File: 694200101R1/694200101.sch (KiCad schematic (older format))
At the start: 262 parts, among them J1 USB4085-GF-A, J2 Conn_01x05_Male, J3 Conn_01x02_Male, SW1 MX_SW, SW10 MX_SW, SW100 MX_SW, SW101 MX_SW, SW102 MX_SW, SW103 MX_SW, SW104 MX_SW, SW105 MX_SW, SW106 MX_SW, SW107 MX_SW, SW11 MX_SW, SW12 MX_SW, SW13 MX_SW, SW14 MX_SW, SW15 MX_SW, SW16 MX_SW, SW17 MX_SW, SW18 MX_SW, SW19 MX_SW, SW2 MX_SW, SW20 MX_SW, SW21 MX_SW, SW22 MX_SW, SW23 MX_SW, SW24 MX_SW, SW25 MX_SW, SW26 MX_SW, SW27 MX_SW, SW28 MX_SW, SW29 MX_SW, SW3 MX_SW, SW30 MX_SW, SW31 MX_SW, SW32 MX_SW, SW33 MX_SW, SW34 MX_SW, SW35 MX_SW, SW36 MX_SW, SW37 MX_SW, SW38 MX_SW, SW39 MX_SW, SW4 MX_SW, SW40 MX_SW, SW41 MX_SW, SW42 MX_SW, SW43 MX_SW, SW44 MX_SW, SW45 MX_SW, SW46 MX_SW, SW47 MX_SW, SW48 MX_SW, SW49 MX_SW, SW5 MX_SW, SW50 MX_SW, SW51 MX_SW, SW52 MX_SW, SW53 MX_SW, SW54 MX_SW, SW55 MX_SW, SW56 MX_SW, SW57 MX_SW, SW58 MX_SW, SW59 MX_SW, SW6 MX_SW, SW60 MX_SW, SW61 MX_SW, SW62 MX_SW, SW63 MX_SW, SW64 MX_SW, SW65 MX_SW, SW66 MX_SW, SW67 MX_SW, SW68 MX_SW, SW69 MX_SW, SW7 MX_SW, SW70 MX_SW, SW71 MX_SW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

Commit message: fucking ship it
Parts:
- gave numbers to parts that had none: 1
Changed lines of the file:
@@
 RST
 $Comp
-L capacitor-lib:CL21A475KAQNNNE C?
+L capacitor-lib:CL21A475KAQNNNE C25
 U 1 1 609A6D18
 P 2850 9500
-F 0 "C?" H 2978 9446 50  0000 L CNN
+F 0 "C25" H 2978 9446 50  0000 L CNN
 F 1 "CL21A475KAQNNNE" H 2850 9700 50  0001 L CNN
 F 2 "Capacitor_SMD:C_0805_2012Metric" H 2850 9800 50  0001 L CNN

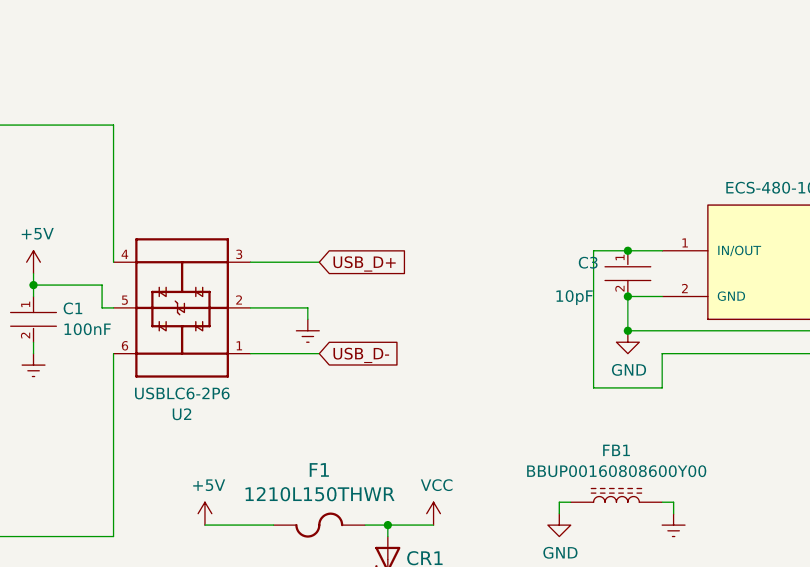
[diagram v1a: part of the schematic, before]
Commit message: Added 0 Ohm resistors for USB Data lines
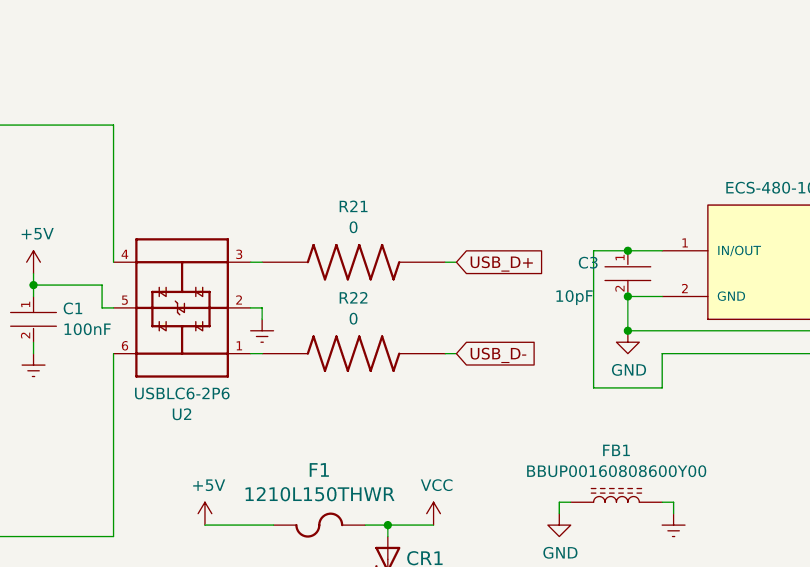
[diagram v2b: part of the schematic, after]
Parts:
- added R21, R22: MCT06030Z0000ZP500, Resistor-Libs:RESC1508X55N, symbol Resistor-Lib:MCT06030Z0000ZP500
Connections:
- net USB_D+: now also R21.2; no longer U2.3
- net USB_D-: now also R22.2; no longer U2.1
- new net: R22.1, U2.1
- new net: R21.1, U2.3
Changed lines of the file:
@@
 Wire Wire Line
 	2400 7950 2400 8950
-Text GLabel 4250 7350 2    50   Input ~ 0
+Text GLabel 4850 7350 2    50   Input ~ 0
 USB_D+
-Text GLabel 4250 7750 2    50   Input ~ 0
+Text GLabel 4850 7750 2    50   Input ~ 0
 USB_D-
 Connection ~ 2400 6350
@@
 $EndComp
 Wire Wire Line
-	4250 7350 3950 7350
+	4000 7350 3950 7350
 Wire Wire Line
-	4200 7550 4200 7600
+	4000 7550 4000 7600
 $Comp
 L capacitor-lib:06035A100JAT2A C6
@@
 $EndComp
 Wire Wire Line
-	3950 7550 4200 7550
+	3950 7550 4000 7550
 $Comp
 L capacitor-lib:CL10B104KB8NNNL C1
@@
 L power:Earth #PWR0105
 U 1 1 6042522C
-P 4200 7600
-F 0 "#PWR0105" H 4200 7350 50  0001 C CNN
-F 1 "Earth" H 4200 7450 50  0001 C CNN
-F 2 "" H 4200 7600 50  0001 C CNN
-F 3 "~" H 4200 7600 50  0001 C CNN
-	1    4200 7600
+P 4000 7600
+F 0 "#PWR0105" H 4000 7350 50  0001 C CNN
+F 1 "Earth" H 4000 7450 50  0001 C CNN
+F 2 "" H 4000 7600 50  0001 C CNN
+F 3 "~" H 4000 7600 50  0001 C CNN
+	1    4000 7600
 	1    0    0    -1
 $EndComp
 Wire Wire Line
-	3950 7750 4250 7750
+	3950 7750 4000 7750
 $Comp
 L power:Earth #PWR0106
@@
 	2850 9400 3250 9400
 Connection ~ 3250 9400
+$Comp
+L Resistor-Lib:MCT06030Z0000ZP500 R21
+U 1 1 609B13D9
+P 4400 7350
+F 0 "R21" H 4400 7592 50  0000 C CNN
+F 1 "MCT06030Z0000ZP500" H 4100 7150 50  0001 L BNN
+F 2 "Resistor-Libs:RESC1508X55N" H 4400 7350 50  0001 L BNN
+F 3 "" H 4400 7350 50  0001 L BNN
+F 4 "0" H 4400 7501 50  0000 C CNN "resistance"
+	1    4400 7350
+	1    0    0    -1
+$EndComp
+$Comp
+L Resistor-Lib:MCT06030Z0000ZP500 R22
+U 1 1 609B3AF3
+P 4400 7750
+F 0 "R22" H 4400 7992 50  0000 C CNN
+F 1 "MCT06030Z0000ZP500" H 4100 7550 50  0001 L BNN
+F 2 "Resistor-Libs:RESC1508X55N" H 4400 7750 50  0001 L BNN
+F 3 "" H 4400 7750 50  0001 L BNN
+F 4 "0" H 4400 7901 50  0000 C CNN "resistance"
+	1    4400 7750
+	1    0    0    -1
+$EndComp
+Wire Wire Line
+	4800 7350 4850 7350
+Wire Wire Line
+	4800 7750 4850 7750
 $EndSCHEMATC

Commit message: round 1 of stupid data resistors
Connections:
- net USB-: now reaches R22.1, U2.1
- net USB+: now reaches R21.1, U2.3
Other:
- moved on the sheet: R21, R22
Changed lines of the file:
@@
 Wire Wire Line
 	2400 7950 2400 8950
-Text GLabel 4850 7350 2    50   Input ~ 0
+Text GLabel 4950 7350 2    50   Input ~ 0
 USB_D+
-Text GLabel 4850 7750 2    50   Input ~ 0
+Text GLabel 4950 7750 2    50   Input ~ 0
 USB_D-
 Connection ~ 2400 6350
@@
 $EndComp
 Wire Wire Line
-	4000 7350 3950 7350
-Wire Wire Line
 	4000 7550 4000 7600
 $Comp
@@
 	1    0    0    -1
 $EndComp
-Wire Wire Line
-	3950 7750 4000 7750
 $Comp
 L power:Earth #PWR0106
@@
 L Resistor-Lib:MCT06030Z0000ZP500 R21
 U 1 1 609B13D9
-P 4400 7350
-F 0 "R21" H 4400 7592 50  0000 C CNN
-F 1 "MCT06030Z0000ZP500" H 4100 7150 50  0001 L BNN
-F 2 "Resistor-Libs:RESC1508X55N" H 4400 7350 50  0001 L BNN
-F 3 "" H 4400 7350 50  0001 L BNN
-F 4 "0" H 4400 7501 50  0000 C CNN "resistance"
-	1    4400 7350
+P 4500 7350
+F 0 "R21" H 4500 7592 50  0000 C CNN
+F 1 "MCT06030Z0000ZP500" H 4200 7150 50  0001 L BNN
+F 2 "Resistor-Libs:RESC1508X55N" H 4500 7350 50  0001 L BNN
+F 3 "" H 4500 7350 50  0001 L BNN
+F 4 "0" H 4500 7501 50  0000 C CNN "resistance"
+	1    4500 7350
 	1    0    0    -1
 $EndComp
@@
 L Resistor-Lib:MCT06030Z0000ZP500 R22
 U 1 1 609B3AF3
-P 4400 7750
-F 0 "R22" H 4400 7992 50  0000 C CNN
-F 1 "MCT06030Z0000ZP500" H 4100 7550 50  0001 L BNN
-F 2 "Resistor-Libs:RESC1508X55N" H 4400 7750 50  0001 L BNN
-F 3 "" H 4400 7750 50  0001 L BNN
-F 4 "0" H 4400 7901 50  0000 C CNN "resistance"
-	1    4400 7750
+P 4500 7750
+F 0 "R22" H 4500 7992 50  0000 C CNN
+F 1 "MCT06030Z0000ZP500" H 4200 7550 50  0001 L BNN
+F 2 "Resistor-Libs:RESC1508X55N" H 4500 7750 50  0001 L BNN
+F 3 "" H 4500 7750 50  0001 L BNN
+F 4 "0" H 4500 7901 50  0000 C CNN "resistance"
+	1    4500 7750
 	1    0    0    -1
 $EndComp
 Wire Wire Line
-	4800 7350 4850 7350
+	4900 7350 4950 7350
+Wire Wire Line
+	4900 7750 4950 7750
+Wire Wire Line
+	3950 7350 4100 7350
 Wire Wire Line
-	4800 7750 4850 7750
+	3950 7750 4100 7750
+Text Label 4000 7350 0    50   ~ 0
+USB+
+Text Label 4050 7750 0    50   ~ 0
+USB-
 $EndSCHEMATC

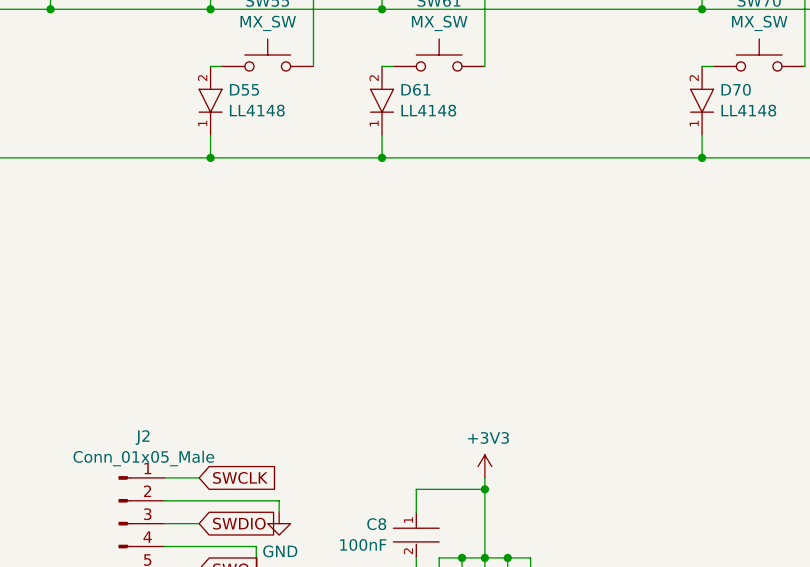
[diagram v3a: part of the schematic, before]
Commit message: Added Logo to PCB
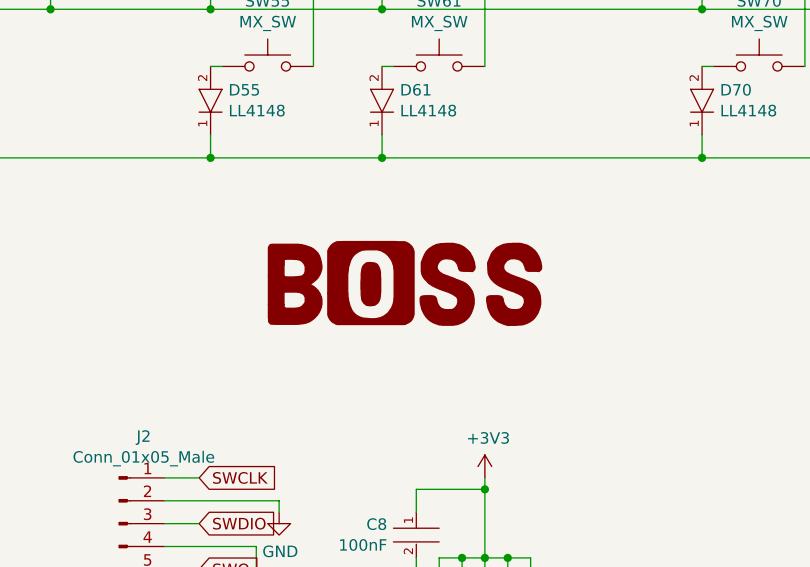
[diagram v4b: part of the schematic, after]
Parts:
- added G1: LOGO, BossLogo:BossLogo, symbol BossLogo:LOGO
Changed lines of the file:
@@
 Text Label 4050 7750 0    50   ~ 0
 USB-
+$Comp
+L BossLogo:LOGO G1
+U 1 1 608F531A
+P 8600 5100
+F 0 "G1" H 8600 4532 60  0001 C CNN
+F 1 "LOGO" H 8600 5668 60  0001 C CNN
+F 2 "BossLogo:BossLogo" H 8600 5100 50  0001 C CNN
+F 3 "" H 8600 5100 50  0001 C CNN
+	1    8600 5100
+	1    0    0    -1
+$EndComp
 $EndSCHEMATC

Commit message: Revert "Added Logo to PCB"
This reverts commit c429ff769e35cd6cf0a76a8cfb685bedc6b738e9.
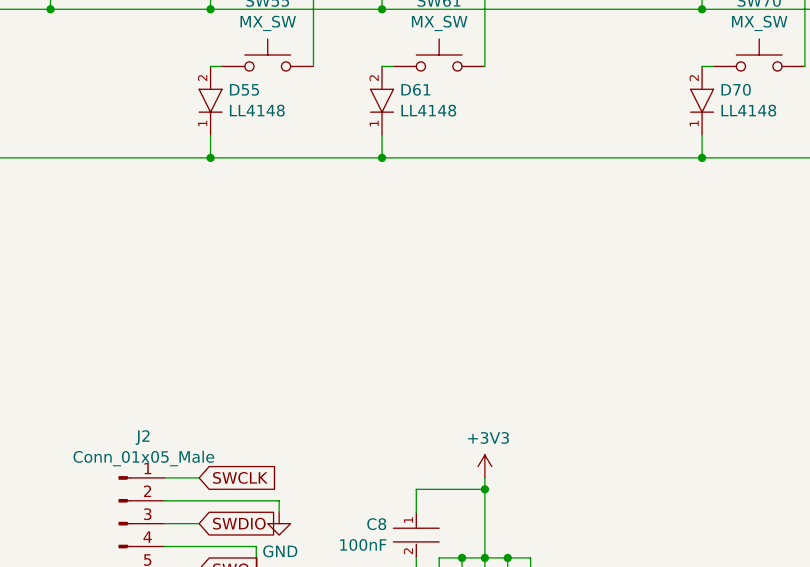
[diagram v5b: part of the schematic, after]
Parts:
- removed G1: LOGO, BossLogo:BossLogo, symbol BossLogo:LOGO
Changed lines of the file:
@@
 Text Label 4050 7750 0    50   ~ 0
 USB-
-$Comp
-L BossLogo:LOGO G1
-U 1 1 608F531A
-P 8600 5100
-F 0 "G1" H 8600 4532 60  0001 C CNN
-F 1 "LOGO" H 8600 5668 60  0001 C CNN
-F 2 "BossLogo:BossLogo" H 8600 5100 50  0001 C CNN
-F 3 "" H 8600 5100 50  0001 C CNN
-	1    8600 5100
-	1    0    0    -1
-$EndComp
 $EndSCHEMATC

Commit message: Added Logo Again......
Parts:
- added G1: LOGO, BossLogo:BossLogo, symbol 694200101-rescue:LOGO-BossLogo
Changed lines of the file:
@@
 Text Label 4050 7750 0    50   ~ 0
 USB-
+$Comp
+L 694200101-rescue:LOGO-BossLogo G1
+U 1 1 608F531A
+P 8600 5100
+F 0 "G1" H 8600 4532 60  0001 C CNN
+F 1 "LOGO" H 8600 5668 60  0001 C CNN
+F 2 "BossLogo:BossLogo" H 8600 5100 50  0001 C CNN
+F 3 "" H 8600 5100 50  0001 C CNN
+	1    8600 5100
+	1    0    0    -1
+$EndComp
 $EndSCHEMATC

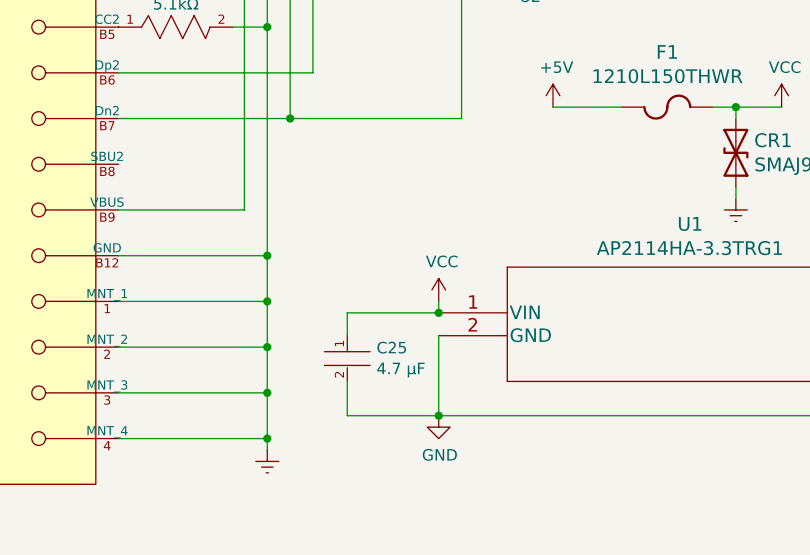
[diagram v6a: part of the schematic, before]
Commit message: fixed power to led drivers
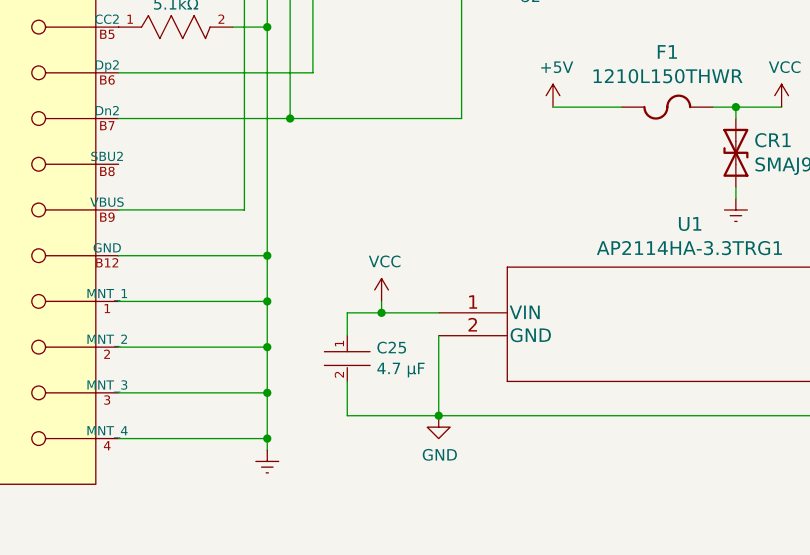
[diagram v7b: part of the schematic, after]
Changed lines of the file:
@@
 	4550 8500 4750 8500
-$Comp
-L power:VCC #PWR0102
-U 1 1 601DBF47
-P 3250 9350
-F 0 "#PWR0102" H 3250 9200 50  0001 C CNN
-F 1 "VCC" H 3265 9523 50  0000 C CNN
-F 2 "" H 3250 9350 50  0001 C CNN
-F 3 "" H 3250 9350 50  0001 C CNN
-	1    3250 9350
-	1    0    0    -1
-$EndComp
-Wire Wire Line
-	3250 9350 3250 9400
 $Comp
 L Littlefuse:SMAJ9.0CA CR1
@@
 $EndComp
 Wire Wire Line
-	5450 9500 5850 9500
-Wire Wire Line
-	5500 9850 5500 9400
-$Comp
-L DI-LVO:AP2114HA-3.3TRG1 U1
-U 1 1 5FF9E77D
-P 3250 9400
-F 0 "U1" H 4350 9787 60  0000 C CNN
-F 1 "AP2114HA-3.3TRG1" H 4350 9681 60  0000 C CNN
-F 2 "DI-LVO:AP2114HA-3.3TRG1" H 4350 9640 60  0001 C CNN
-F 3 "" H 3250 9400 60  0000 C CNN
-	1    3250 9400
-	1    0    0    -1
-$EndComp
-Wire Wire Line
 	2850 9700 2850 9850
 Wire Wire Line
@@
 	2850 9500 2850 9400
 Wire Wire Line
-	2850 9400 3250 9400
-Connection ~ 3250 9400
+	2850 9400 3000 9400
 $Comp
 L Resistor-Lib:MCT06030Z0000ZP500 R21
@@
 	1    0    0    -1
 $EndComp
+Wire Wire Line
+	5450 9500 5850 9500
+Wire Wire Line
+	5500 9850 5500 9400
+$Comp
+L DI-LVO:AP2114HA-3.3TRG1 U1
+U 1 1 5FF9E77D
+P 3250 9400
+F 0 "U1" H 4350 9787 60  0000 C CNN
+F 1 "AP2114HA-3.3TRG1" H 4350 9681 60  0000 C CNN
+F 2 "DI-LVO:AP2114HA-3.3TRG1" H 4350 9640 60  0001 C CNN
+F 3 "" H 3250 9400 60  0000 C CNN
+	1    3250 9400
+	1    0    0    -1
+$EndComp
+$Comp
+L power:VCC #PWR0102
+U 1 1 601DBF47
+P 3000 9350
+F 0 "#PWR0102" H 3000 9200 50  0001 C CNN
+F 1 "VCC" H 3015 9523 50  0000 C CNN
+F 2 "" H 3000 9350 50  0001 C CNN
+F 3 "" H 3000 9350 50  0001 C CNN
+	1    3000 9350
+	1    0    0    -1
+$EndComp
+Wire Wire Line
+	3000 9350 3000 9400
+Connection ~ 3000 9400
+Wire Wire Line
+	3000 9400 3250 9400
 $EndSCHEMATC

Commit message: Updated USB C Connector
Connector didn't have proper soldermask so we need to use a proper footprint that is compatible
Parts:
- J1: footprint eec-GCT:Global_Connector_Technology-USB4085-GF-A-MFG -> Connector_USB:USB_C_Receptacle_GCT_USB4085
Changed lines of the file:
@@
 F 0 "J1" H 1222 4296 50  0000 R CNN
 F 1 "USB4085-GF-A" H 1222 4205 50  0000 R CNN
-F 2 "eec-GCT:Global_Connector_Technology-USB4085-GF-A-MFG" H 1950 6650 50  0001 L CNN
+F 2 "Connector_USB:USB_C_Receptacle_GCT_USB4085" H 1950 6650 50  0001 L CNN
 F 3 "https://gct.co/files/drawings/usb4085.pdf" H 1950 6750 50  0001 L CNN
 F 4 "No" H 1950 6850 50  0001 L CNN "automotive"
